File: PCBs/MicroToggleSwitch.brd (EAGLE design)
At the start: 15 x 40.1 mm, 3 parts

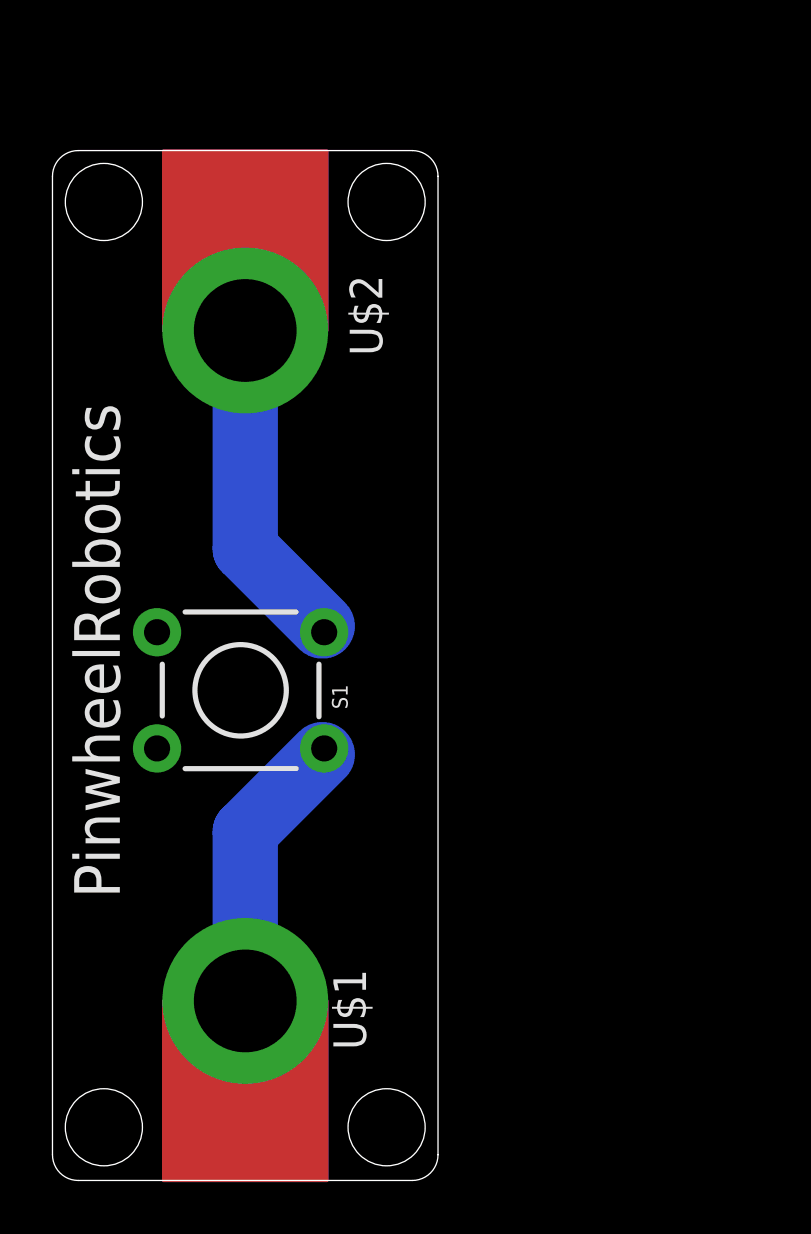
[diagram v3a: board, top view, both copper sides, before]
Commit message: Dimension added
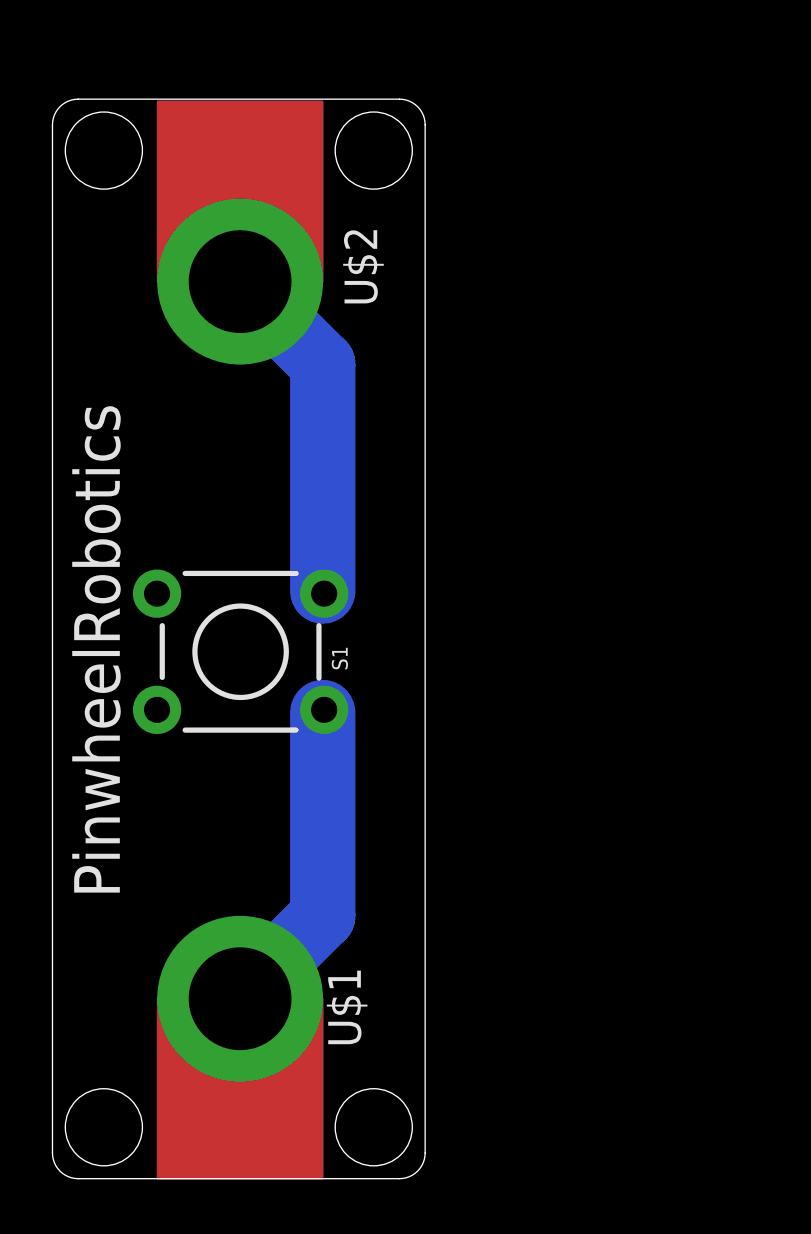
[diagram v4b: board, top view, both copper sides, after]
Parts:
- moved U$2 1.91 mm to (7.30, 34.9)
- moved S1 1.50 mm to (7.32, 20.5)
- moved U$1 0.22 mm to (7.30, 7.00)
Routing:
- net N$1: track 11.1 -> 12.6 mm
- net N$2: track 13.0 -> 13.5 mm
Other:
- board size 15 x 40.1 mm -> 14.5 x 42 mm
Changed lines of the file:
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@@
 <board>
 <plain>
-<wire x1="0" y1="39" x2="0" y2="0.93" width="0" layer="20"/>
-<wire x1="0" y1="0.93" x2="1" y2="-0.07" width="0" layer="20" curve="90"/>
-<wire x1="1" y1="-0.07" x2="14" y2="-0.07" width="0" layer="20"/>
-<wire x1="14" y1="-0.07" x2="15" y2="0.93" width="0" layer="20" curve="90"/>
-<wire x1="15" y1="0.93" x2="15" y2="39" width="0" layer="20"/>
-<wire x1="15" y1="39" x2="14" y2="40" width="0" layer="20" curve="90"/>
-<wire x1="14" y1="40" x2="1" y2="40" width="0" layer="20"/>
-<wire x1="1" y1="40" x2="0" y2="39" width="0" layer="20" curve="90"/>
-<hole x="2" y="38" drill="3"/>
-<hole x="13" y="38" drill="3"/>
+<wire x1="0" y1="41" x2="0" y2="1" width="0" layer="20"/>
+<wire x1="0" y1="1" x2="1" y2="0" width="0" layer="20" curve="90"/>
+<wire x1="1" y1="0" x2="13.5" y2="0" width="0" layer="20"/>
+<wire x1="13.5" y1="0" x2="14.5" y2="1" width="0" layer="20" curve="90"/>
+<wire x1="14.5" y1="1" x2="14.5" y2="41" width="0" layer="20"/>
+<wire x1="14.5" y1="41" x2="13.5" y2="42" width="0" layer="20" curve="90"/>
+<wire x1="13.5" y1="42" x2="1" y2="42" width="0" layer="20"/>
+<wire x1="1" y1="42" x2="0" y2="41" width="0" layer="20" curve="90"/>
+<hole x="2" y="40" drill="3"/>
+<hole x="12.5" y="40" drill="3"/>
 <hole x="2" y="2" drill="3"/>
-<hole x="13" y="2" drill="3"/>
+<hole x="12.5" y="2" drill="3"/>
 <text x="2.621" y="10.915" size="1.778" layer="21" rot="R90">PinwheelRobotics </text>
-<text x="14.051" y="30.457" size="1.778" layer="22" rot="MR270">care@pinwheel.in</text>
+<text x="13.551" y="29.457" size="1.778" layer="22" rot="MR270">care@pinwheel.in</text>
 </plain>
 <attributes>
@@
 </autorouter>
 <elements>
-<element name="S1" library="SparkFun-Switches" library_urn="urn:adsk.eagle:library:535" package="TACTILE_SWITCH_PTH_6.0MM" package3d_urn="urn:adsk.eagle:package:40163/1" value="MOMENTARY-SWITCH-SPST-PTH-6.0MM" x="7.32" y="19" smashed="yes" rot="R180">
-<attribute name="NAME" x="10.876" y="18.746" size="0.6096" layer="25" font="vector" ratio="20" rot="R270" align="bottom-center"/>
-<attribute name="PROD_ID" value=" SWCH-08441" x="-14.27" y="54.56" size="1.778" layer="27" rot="R180" display="off"/>
-<attribute name="SF_SKU" value="COM-00097" x="-14.27" y="54.56" size="1.778" layer="27" rot="R180" display="off"/>
+<element name="S1" library="SparkFun-Switches" library_urn="urn:adsk.eagle:library:535" package="TACTILE_SWITCH_PTH_6.0MM" package3d_urn="urn:adsk.eagle:package:40163/1" value="MOMENTARY-SWITCH-SPST-PTH-6.0MM" x="7.32" y="20.5" smashed="yes" rot="R180">
+<attribute name="NAME" x="10.876" y="20.246" size="0.6096" layer="25" font="vector" ratio="20" rot="R270" align="bottom-center"/>
+<attribute name="PROD_ID" value=" SWCH-08441" x="-14.27" y="56.06" size="1.778" layer="27" rot="R180" display="off"/>
+<attribute name="SF_SKU" value="COM-00097" x="-14.27" y="56.06" size="1.778" layer="27" rot="R180" display="off"/>
 </element>
-<element name="U$1" library="microbit" package="MICROBIT_PAD" value="MICROBIT_PAD" x="7.5" y="6.915" smashed="yes">
-<attribute name="NAME" x="12.199" y="5.01" size="1.27" layer="21" rot="R90"/>
+<element name="U$1" library="microbit" package="MICROBIT_PAD" value="MICROBIT_PAD" x="7.3" y="7" smashed="yes">
+<attribute name="NAME" x="11.999" y="5.095" size="1.27" layer="21" rot="R90"/>
 </element>
-<element name="U$2" library="microbit" package="MICROBIT_PAD" value="MICROBIT_PAD" x="7.5" y="33" smashed="yes" rot="R180">
-<attribute name="NAME" x="11.564" y="35.159" size="1.27" layer="21" rot="R270"/>
+<element name="U$2" library="microbit" package="MICROBIT_PAD" value="MICROBIT_PAD" x="7.3" y="34.9" smashed="yes" rot="R180">
+<attribute name="NAME" x="11.364" y="37.059" size="1.27" layer="21" rot="R270"/>
 </element>
 </elements>
@@
 <contactref element="U$1" pad="PAD"/>
 <contactref element="S1" pad="1"/>
-<wire x1="7.5" y1="13.5" x2="10.5" y2="16.5" width="2.54" layer="16"/>
-<wire x1="7.5" y1="6.915" x2="7.5" y2="13.5" width="2.54" layer="16"/>
-<wire x1="10.5" y1="16.5" x2="10.5712" y2="16.7394" width="0.1524" layer="16"/>
+<wire x1="10.5156" y1="10.2108" x2="10.5156" y2="18.1356" width="2.54" layer="16"/>
+<wire x1="7.3152" y1="7.0104" x2="10.5156" y2="10.2108" width="2.54" layer="16"/>
+<wire x1="10.5156" y1="18.1356" x2="10.5712" y2="18.2394" width="0.1524" layer="16"/>
+<wire x1="7.3152" y1="7.0104" x2="7.3" y2="7" width="0.1524" layer="16"/>
 </signal>
 <signal name="N$2">
 <contactref element="U$2" pad="PAD"/>
 <contactref element="S1" pad="3"/>
-<wire x1="7.5" y1="24.5" x2="10.5" y2="21.5" width="2.54" layer="16"/>
-<wire x1="7.5" y1="33" x2="7.5" y2="24.5" width="2.54" layer="16"/>
-<wire x1="10.5" y1="21.5" x2="10.5712" y2="21.2606" width="0.1524" layer="16"/>
+<wire x1="10.5156" y1="31.6992" x2="10.5156" y2="22.86" width="2.54" layer="16"/>
+<wire x1="7.3152" y1="34.8996" x2="10.5156" y2="31.6992" width="2.54" layer="16"/>
+<wire x1="10.5156" y1="22.86" x2="10.5712" y2="22.7606" width="0.1524" layer="16"/>
+<wire x1="7.3152" y1="34.8996" x2="7.3" y2="34.9" width="0.1524" layer="16"/>
 </signal>
 </signals>
